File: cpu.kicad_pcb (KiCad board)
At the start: 2 copper layers, 179.6 x 119 mm, 52 parts, among them J1 LCD 2004 Female Header, J2 UJC-HP-3-SMT-TR, SW1 TL2230, U1 LM555, U10 SST39SF040-70-4C-PHE, U2 74LS00, U3 LM555, U4 74LS163, U5 74LS163, U6 74LS163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

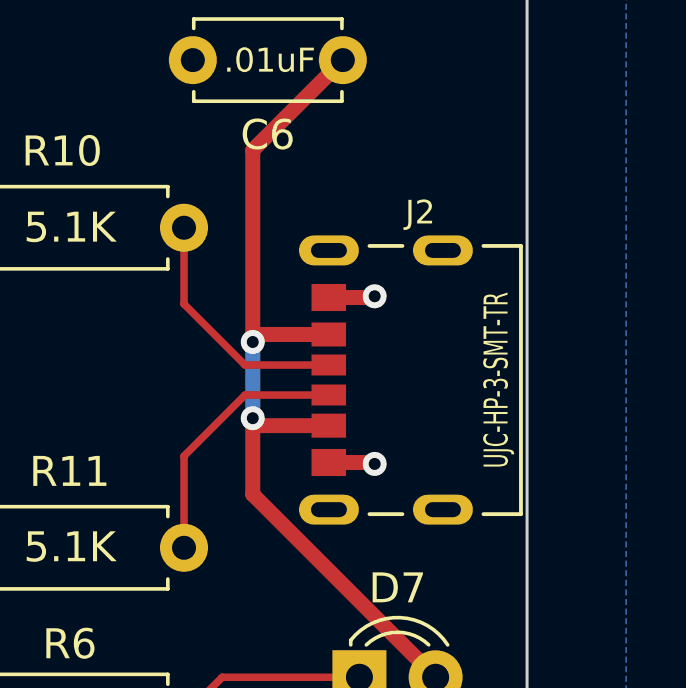
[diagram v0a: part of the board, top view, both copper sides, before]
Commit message: Updated symbols/footprint for USB and 5K Trimmer Pots.
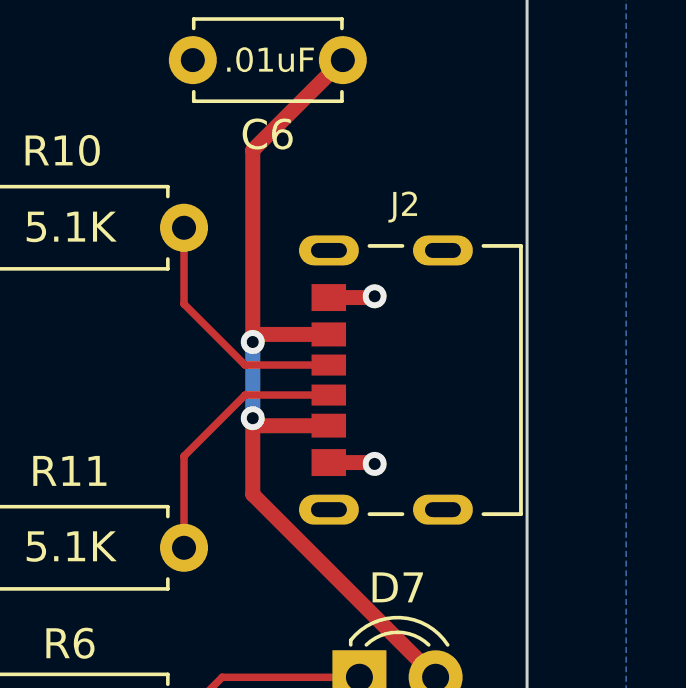
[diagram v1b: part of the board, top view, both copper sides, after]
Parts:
- J2: footprint footprints:CUI_UJC-HP-3-SMT-TR -> footprints:CUI_UJC-HP-M-G-5-MSMT-TR
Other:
- board text added: "${project_name} Inspired by Ian Ward's Project: 20xt6 Homebrew CPU (https://excess.org/cpu/) PCB designed by an appreciative subscriber to his YouTube channel. Version ${version} 3/19/2024"
- board text removed: "${project_name} Inspired by Ian Ward (www excess.org) YouTube Channel: https://www.youtube.com/@IanWard1 PCB designed by one of his appreciative YouTube subscribers. Version ${version} 3/17/2024"
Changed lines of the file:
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@@
     )
   )
-  (footprint "footprints:CUI_UJC-HP-3-SMT-TR" (layer "F.Cu")
+  (footprint "footprints:CUI_UJC-HP-M-G-5-MSMT-TR" (layer "F.Cu")
     (at 214.884 122.172 90)
     (property "MANUFACTURER" "CUI Devices")
@@
     (property "Sheetname" "")
     (attr smd)
-    (fp_text reference "J2" (at 5.584 3.043 180) (layer "F.SilkS")
-        (effects (font (size 0.787402 0.787402) (thickness 0.15)))
+    (fp_text reference "J2" (at 5.84 2.54 180) (layer "F.SilkS")
+        (effects (font (size 0.8 0.787402) (thickness 0.15)))
     )
-    (fp_text value "UJC-HP-3-SMT-TR" (at -0.004 5.583 90) (layer "F.SilkS")
-        (effects (font (size 0.8 0.5) (thickness 0.125)))
+    (fp_text value "UJC-HP-3-SMT-TR" (at 5 -2 90) (layer "F.Fab")
+        (effects (font (size 0.787402 0.787402) (thickness 0.15)))
     )
     (fp_line (start -4.47 2.45) (end -4.47 1.35)
@@
     (pad "S4" thru_hole oval (at 4.32 3.8 90) (size 1 2) (drill oval 0.5 1.2) (layers "*.Cu" "*.Mask")
       (net 95 "unconnected-(J2-SHIELD__3-PadS4)") (pinfunction "SHIELD__3") (pintype "passive+no_connect") (solder_mask_margin 0.102))
-    (model "${KIPRJMOD}/libraries/3dmodels/UJC-HP-3-SMT-TR.step"
+    (model "${KIPRJMOD}/libraries/3dmodels/CUI_UJC-HP-M-G-5-MSMT-TR.step"
       (offset (xyz 0 0 0))
       (scale (xyz 1 1 1))
@@
   (gr_line (start 144.78 28.448) (end 144.78 100.965)
     (stroke (width 0.2) (type default)) (layer "F.Fab"))
-  (gr_text "${project_name}\nInspired by Ian Ward (www excess.org)\nYouTube Channel: \n	https://www.youtube.com/@IanWard1\nPCB designed by one of his \n    appreciative YouTube subscribers.\nVersion ${version}     3/17/2024" (at 112.395 100.965) (layer "B.SilkS")
+  (gr_text "${project_name}\nInspired by Ian Ward's Project: \n	20xt6 Homebrew CPU \n	 (https://excess.org/cpu/)\nPCB designed by an appreciative \n	subscriber to his YouTube channel.\nVersion ${version}     3/19/2024" (at 108.204 101.092) (layer "B.SilkS")
     (effects (font (size 2 2) (thickness 0.15)) (justify left bottom mirror))
   )

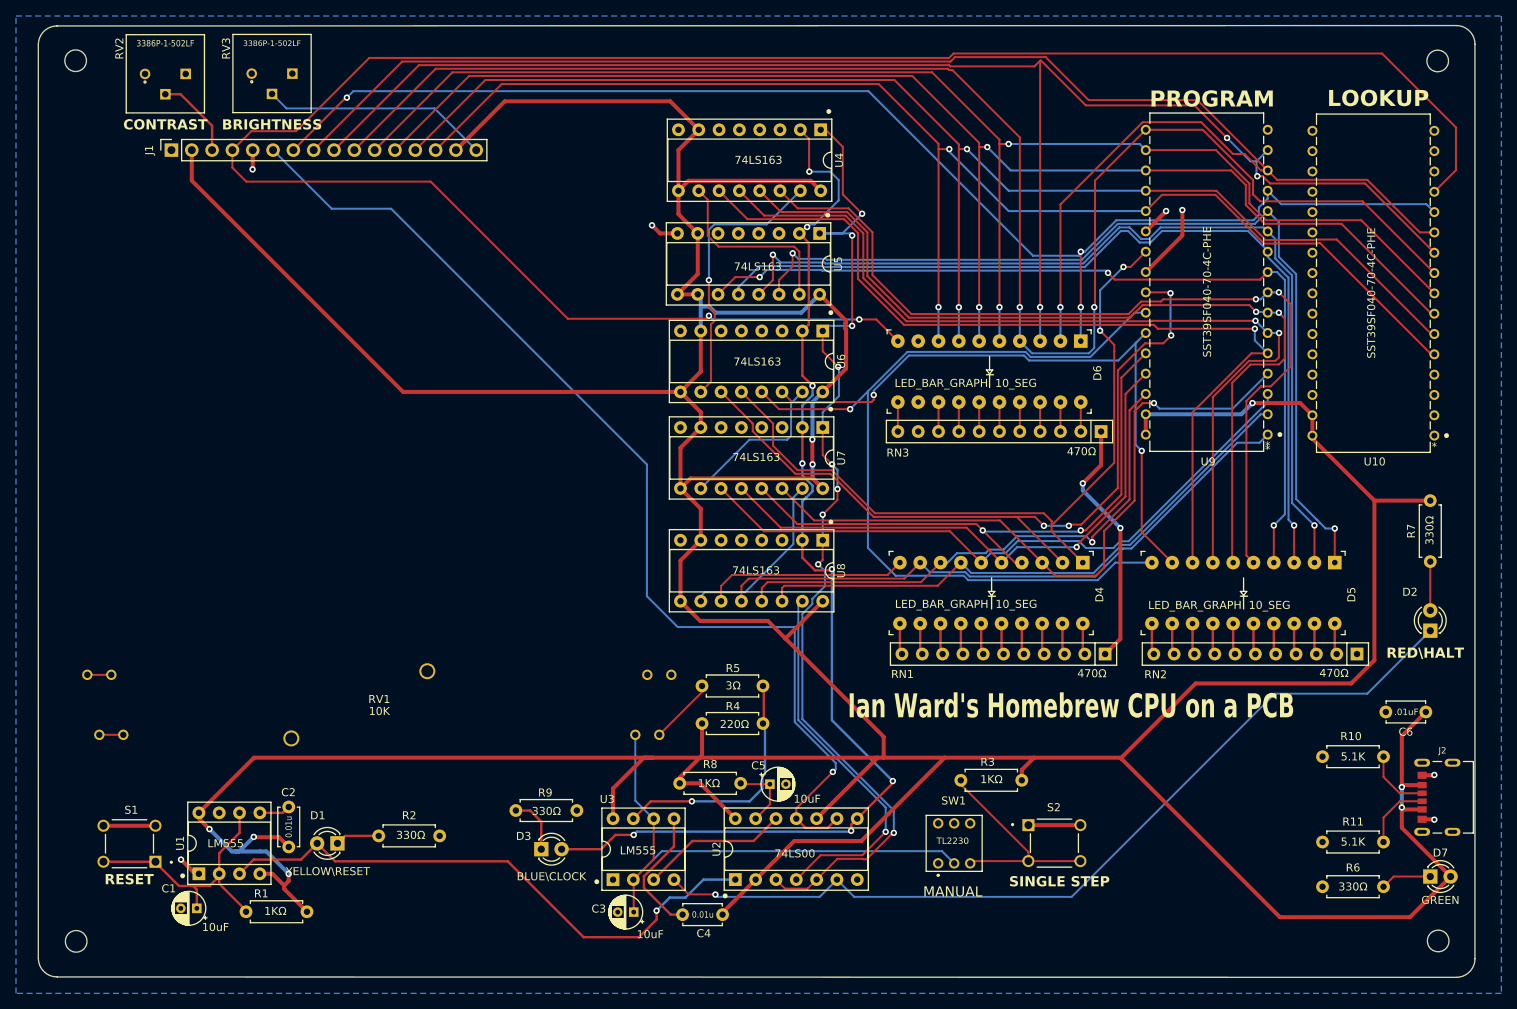
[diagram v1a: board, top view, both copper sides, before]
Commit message: Final changes around adding BOM to README.md
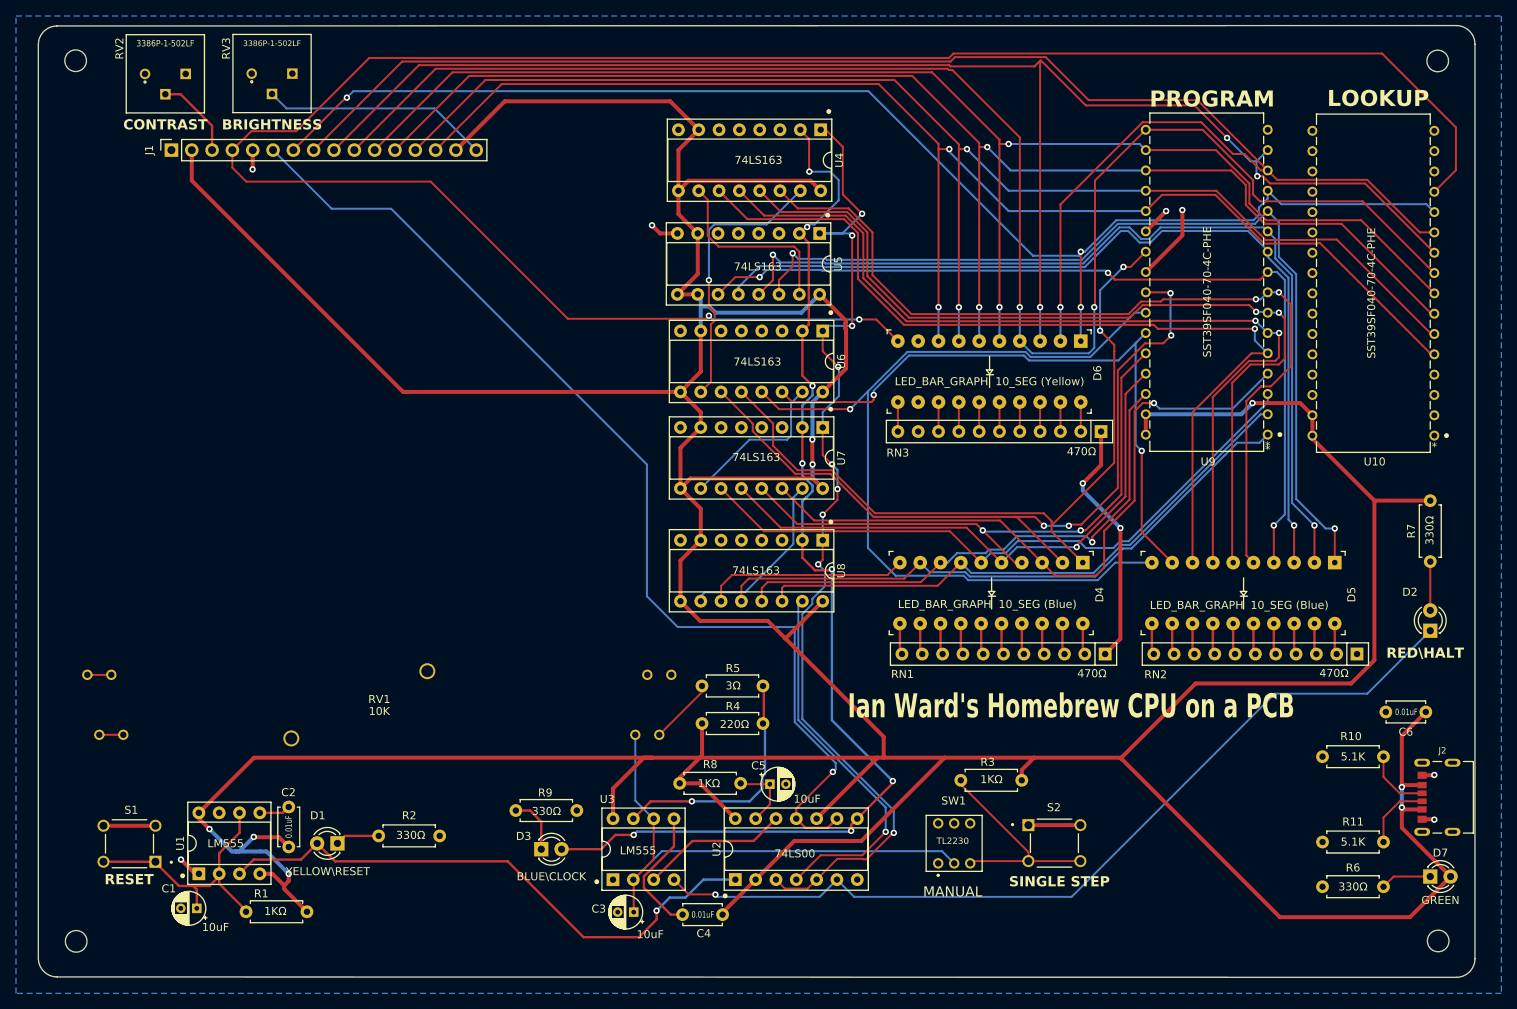
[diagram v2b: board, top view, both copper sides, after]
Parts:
- C2, C4: value 0.01u -> 0.01uF
- C6: value .01uF -> 0.01uF
- D4, D5: value LED_BAR_GRAPH 10_SEG -> LED_BAR_GRAPH 10_SEG (Blue)
- D6: value LED_BAR_GRAPH 10_SEG -> LED_BAR_GRAPH 10_SEG (Yellow)
- J2: value UJC-HP-3-SMT-TR -> CUI_UJC-HP-M-G-5-MSMT-TR
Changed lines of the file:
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@@
         (effects (font (size 1 1) (thickness 0.15)))
     )
-    (fp_text value ".01uF" (at 2.438 -0.014) (layer "F.SilkS")
-        (effects (font (size 0.8 0.8) (thickness 0.15)))
+    (fp_text value "0.01uF" (at 2.438 -0.014) (layer "F.SilkS")
+        (effects (font (size 0.8 0.6) (thickness 0.15)))
     )
     (fp_text user "${REFERENCE}" (at 2.5 0) (layer "F.Fab")
@@
     (property "Sheetfile" "cpu.kicad_sch")
     (property "Sheetname" "")
+    (property "Sim.Enable" "0")
+    (property "exclude_from_bom" "")
     (property "ki_description" "Mounting Hole without connection")
     (property "ki_keywords" "mounting hole")
-    (attr exclude_from_pos_files)
+    (attr exclude_from_pos_files exclude_from_bom)
     (fp_text reference "H3" (at 4.14 -2.49) (layer "F.Fab")
         (effects (font (size 1 1) (thickness 0.15)))
@@
         (effects (font (size 0.8 0.787402) (thickness 0.15)))
     )
-    (fp_text value "UJC-HP-3-SMT-TR" (at 5 -2 90) (layer "F.Fab")
+    (fp_text value "CUI_UJC-HP-M-G-5-MSMT-TR" (at 5 -2 90) (layer "F.Fab")
         (effects (font (size 0.787402 0.787402) (thickness 0.15)))
     )
@@
         (effects (font (size 1 1) (thickness 0.15)))
     )
-    (fp_text value "LED_BAR_GRAPH  10_SEG" (at 5.193 14.586) (layer "F.SilkS")
+    (fp_text value "LED_BAR_GRAPH  10_SEG (Blue)" (at 5.207 11.938) (layer "F.SilkS")
         (effects (font (size 1 1) (thickness 0.15)))
     )
@@
     (property "Sheetfile" "cpu.kicad_sch")
     (property "Sheetname" "")
+    (property "Sim.Enable" "0")
+    (property "exclude_from_bom" "")
     (property "ki_description" "Mounting Hole without connection")
     (property "ki_keywords" "mounting hole")
-    (attr exclude_from_pos_files)
+    (attr exclude_from_pos_files exclude_from_bom)
     (fp_text reference "H4" (at -4.11 -2.89) (layer "F.Fab")
         (effects (font (size 1 1) (thickness 0.15)))
@@
     (property "Sheetfile" "cpu.kicad_sch")
     (property "Sheetname" "")
+    (property "Sim.Enable" "0")
+    (property "exclude_from_bom" "")
     (property "ki_description" "Mounting Hole without connection")
     (property "ki_keywords" "mounting hole")
-    (attr exclude_from_pos_files)
+    (attr exclude_from_pos_files exclude_from_bom)
     (fp_text reference "H1" (at 3.4376 2.9268) (layer "F.Fab")
         (effects (font (size 1 1) (thickness 0.15)))
@@
         (effects (font (size 1 1) (thickness 0.15)))
     )
-    (fp_text value "LED_BAR_GRAPH  10_SEG" (at 5.323 14.432 180) (layer "F.SilkS")
+    (fp_text value "LED_BAR_GRAPH  10_SEG (Blue)" (at 5.323 11.938 180) (layer "F.SilkS")
         (effects (font (size 1 1) (thickness 0.15)))
     )
@@
         (effects (font (size 1 1) (thickness 0.15)))
     )
-    (fp_text value "0.01u" (at 2.49 -0.01 90) (layer "F.SilkS")
-        (effects (font (size 0.8 0.7) (thickness 0.15)))
+    (fp_text value "0.01uF" (at 2.49 -0.01 90) (layer "F.SilkS")
+        (effects (font (size 0.8 0.6) (thickness 0.15)))
     )
     (fp_text user "${REFERENCE}" (at 2.5 0 90) (layer "F.Fab")
@@
         (effects (font (size 1 1) (thickness 0.15)))
     )
-    (fp_text value "0.01u" (at 2.53 0.01) (layer "F.SilkS")
-        (effects (font (size 0.8 0.7) (thickness 0.15)))
+    (fp_text value "0.01uF" (at 2.53 0.01) (layer "F.SilkS")
+        (effects (font (size 0.8 0.6) (thickness 0.15)))
     )
     (fp_text user "${REFERENCE}" (at 2.5 0) (layer "F.Fab")
@@
         (effects (font (size 1 1) (thickness 0.15)))
     )
-    (fp_text value "LED_BAR_GRAPH  10_SEG" (at 5.259 14.382) (layer "F.SilkS")
+    (fp_text value "LED_BAR_GRAPH  10_SEG (Yellow)" (at 5.05 11.4) (layer "F.SilkS")
         (effects (font (size 1 1) (thickness 0.15)))
     )
@@
     (property "Sheetfile" "cpu.kicad_sch")
     (property "Sheetname" "")
+    (property "Sim.Enable" "0")
+    (property "exclude_from_bom" "")
     (property "ki_description" "Mounting Hole without connection")
     (property "ki_keywords" "mounting hole")
-    (attr exclude_from_pos_files)
+    (attr exclude_from_pos_files exclude_from_bom)
     (fp_text reference "H2" (at -4.08 1.6) (layer "F.Fab")
         (effects (font (size 1 1) (thickness 0.15)))

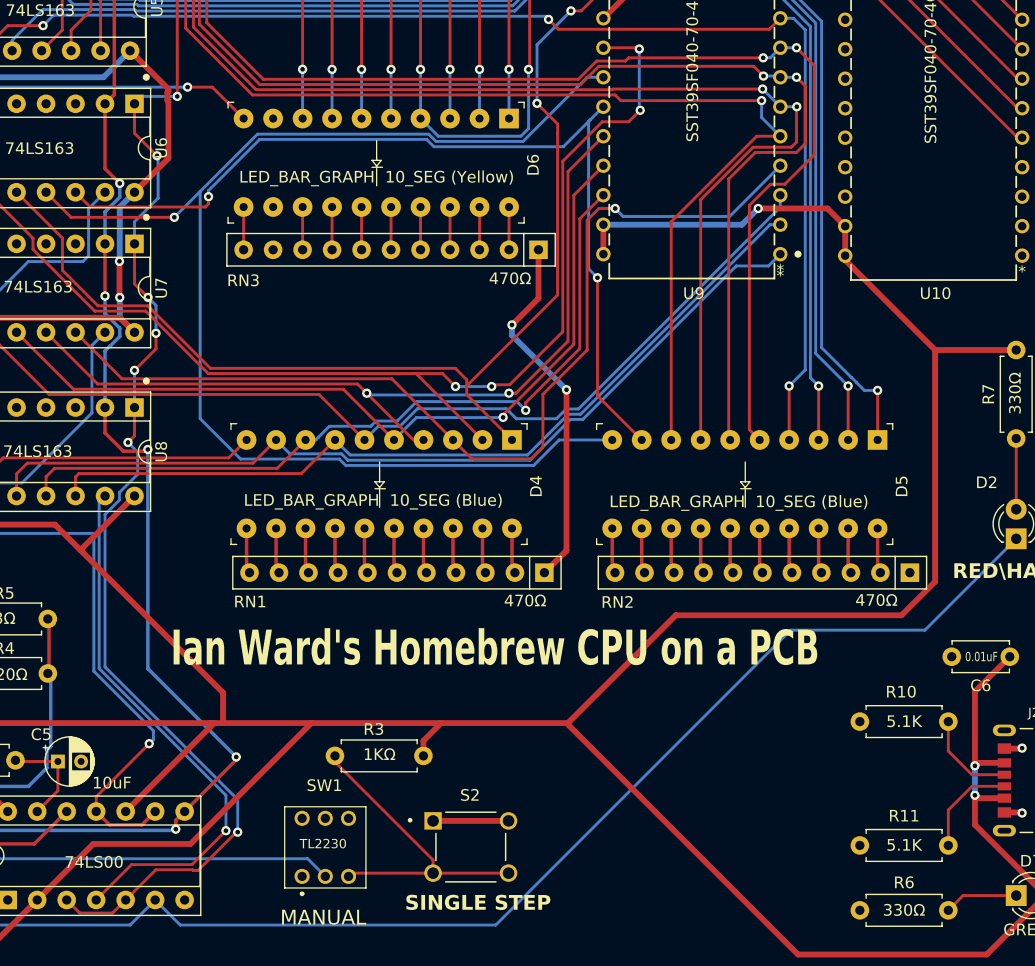
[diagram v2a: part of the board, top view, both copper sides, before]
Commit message: Got rid of track connecting grounds on right side of RN1 and RN2. Regenerated gerber/drill files. Updated board front image.
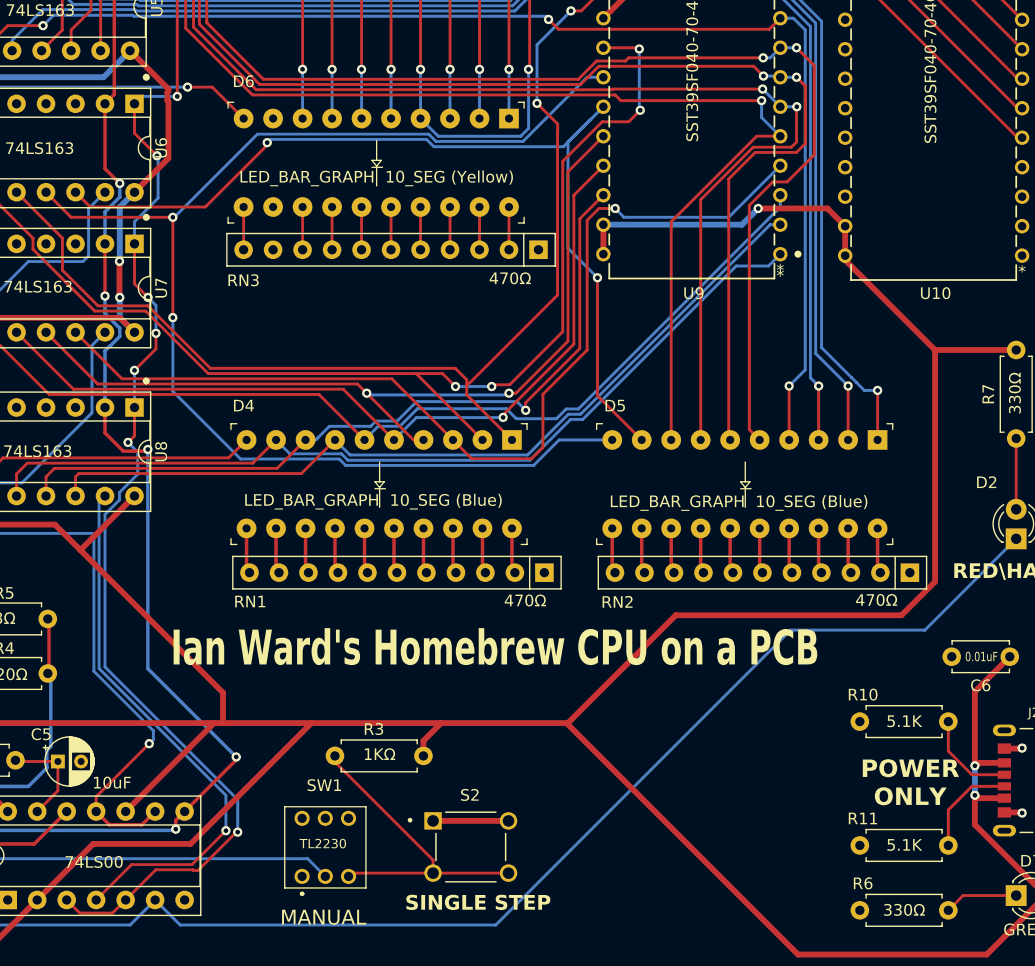
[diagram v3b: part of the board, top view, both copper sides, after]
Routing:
- net GND: track 69.8 -> 38.3 mm, vias 9 -> 7
- net /Counter & Bar Graph/OUT_09: track 112.1 -> 110.8 mm, vias 1 -> 2
- net /Counter & Bar Graph/OUT_08: track 80.3 -> 81.2 mm
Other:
- board text added: "POWER ONLY"
